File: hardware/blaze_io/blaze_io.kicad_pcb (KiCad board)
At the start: 4 copper layers, 70 x 70 mm, 58 parts, among them J1 Conn_01x30_Pin, J2 Conn_01x30_Socket, J3 Conn_01x04, J4 Conn_01x04, J5 Conn_01x03_Pin, J6 Conn_01x03_Pin, J7 Conn_01x03_Pin, J8 Conn_01x03_Pin, J9 JTAG, Q1 AO4892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

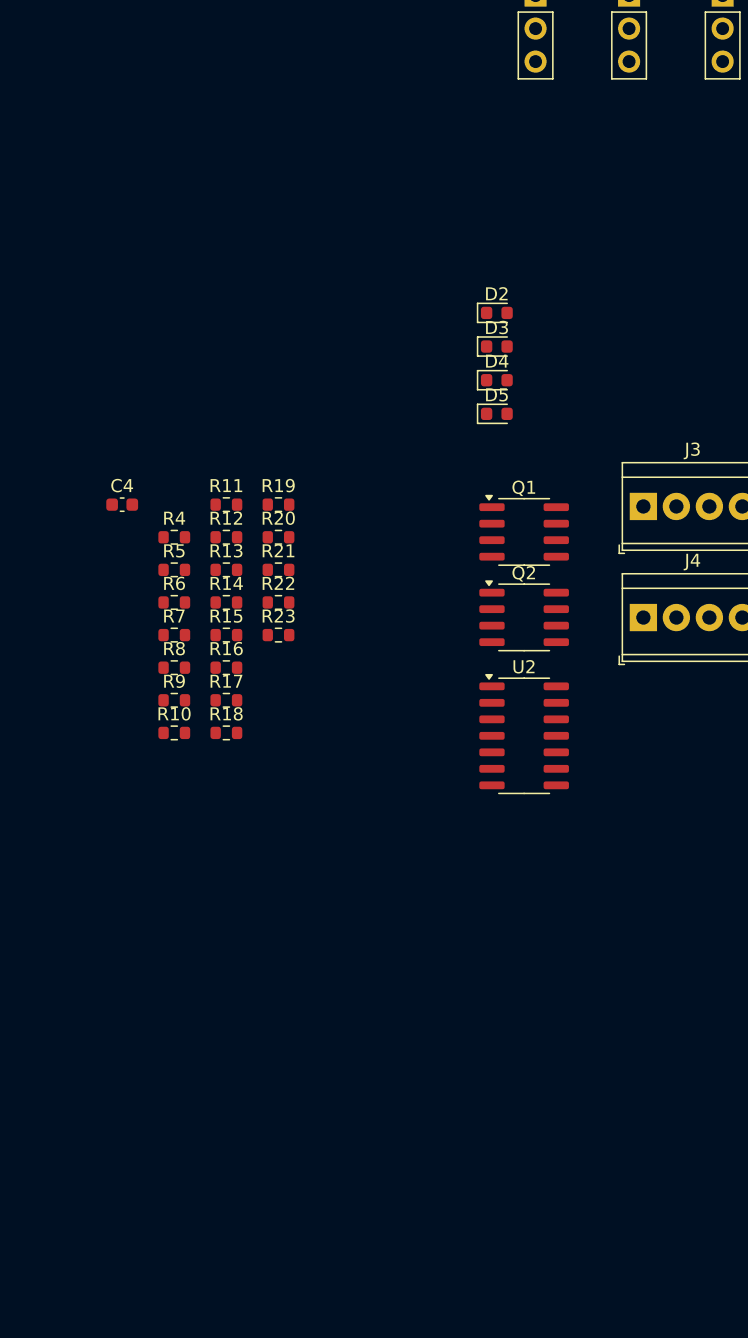
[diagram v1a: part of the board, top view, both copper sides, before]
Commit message: Pyro grouping
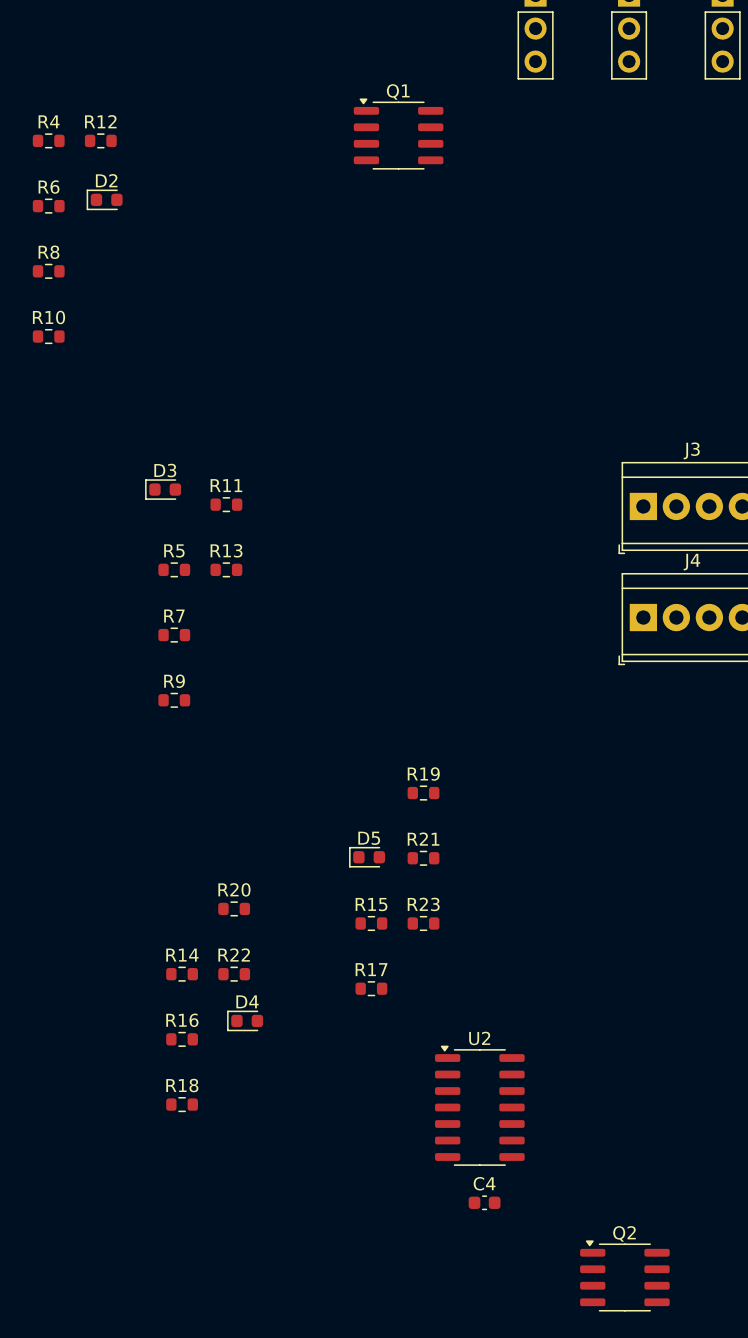
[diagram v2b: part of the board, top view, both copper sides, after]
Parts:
- moved C4 60.5 mm to (48.8, 182.8)
- moved D4 52.9 mm to (30.5, 168.8)
- moved Q2 51.4 mm to (59.6, 188.6)
- moved D5 35.5 mm to (39.9, 156.2)
- moved R8 32.0 mm to (15.2, 111.1)
- moved R6 32.0 mm to (15.2, 106.1)
- moved Q1 32.0 mm to (42.2, 100.7)
- moved R10 32.0 mm to (15.2, 116.1)
- moved R12 32.0 mm to (19.2, 101.1)
- moved R4 32.0 mm to (15.2, 101.1)
- moved D2 31.3 mm to (19.7, 105.6)
- moved U2 28.8 mm to (48.4, 175.5)
- moved R18 28.8 mm to (25.5, 175.2)
- moved R20 28.8 mm to (29.5, 160.2)
- moved R14 28.8 mm to (25.5, 165.2)
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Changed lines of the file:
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@@
 	(footprint "Package_SO:SOIC-8_3.9x4.9mm_P1.27mm"
 		(layer "F.Cu")
-		(at 51.82 131.16)
+		(at 42.155 100.65)
 		(descr "SOIC, 8 Pin (JEDEC MS-012AA, https://www.analog.com/media/en/package-pcb-resources/package/pkg_pdf/soic_narrow-r/r_8.pdf), generated with kicad-footprint-generator ipc_gullwing_generator.py")
 		(tags "SOIC SO")
@@
 	(footprint "Resistor_SMD:R_0603_1608Metric"
 		(layer "F.Cu")
-		(at 28.9 131.57)
+		(at 19.235 101.06)
 		(descr "Resistor SMD 0603 (1608 Metric), square (rectangular) end terminal, IPC_7351 nominal, (Body size source: IPC-SM-782 page 72, https://www.pcb-3d.com/wordpress/wp-content/uploads/ipc-sm-782a_amendment_1_and_2.pdf), generated with kicad-footprint-generator")
 		(tags "resistor")
@@
 	(footprint "Resistor_SMD:R_0603_1608Metric"
 		(layer "F.Cu")
-		(at 32.91 129.06)
+		(at 44.075 151.26)
 		(descr "Resistor SMD 0603 (1608 Metric), square (rectangular) end terminal, IPC_7351 nominal, (Body size source: IPC-SM-782 page 72, https://www.pcb-3d.com/wordpress/wp-content/uploads/ipc-sm-782a_amendment_1_and_2.pdf), generated with kicad-footprint-generator")
 		(tags "resistor")
@@
 	(footprint "LED_SMD:LED_0603_1608Metric"
 		(layer "F.Cu")
-		(at 49.72 114.3)
+		(at 19.6875 105.6)
 		(descr "LED SMD 0603 (1608 Metric), square (rectangular) end terminal, IPC_7351 nominal, (Body size source: http://www.tortai-tech.com/upload/download/2011102023233369053.pdf), generated with kicad-footprint-generator")
 		(tags "LED")
@@
 	(footprint "Resistor_SMD:R_0603_1608Metric"
 		(layer "F.Cu")
-		(at 32.91 136.59)
+		(at 29.5 165.2)
 		(descr "Resistor SMD 0603 (1608 Metric), square (rectangular) end terminal, IPC_7351 nominal, (Body size source: IPC-SM-782 page 72, https://www.pcb-3d.com/wordpress/wp-content/uploads/ipc-sm-782a_amendment_1_and_2.pdf), generated with kicad-footprint-generator")
 		(tags "resistor")
@@
 	(footprint "Resistor_SMD:R_0603_1608Metric"
 		(layer "F.Cu")
-		(at 24.89 136.59)
+		(at 15.225 106.08)
 		(descr "Resistor SMD 0603 (1608 Metric), square (rectangular) end terminal, IPC_7351 nominal, (Body size source: IPC-SM-782 page 72, https://www.pcb-3d.com/wordpress/wp-content/uploads/ipc-sm-782a_amendment_1_and_2.pdf), generated with kicad-footprint-generator")
 		(tags "resistor")
@@
 	(footprint "Package_SO:SOIC-14_3.9x8.7mm_P1.27mm"
 		(layer "F.Cu")
-		(at 51.82 146.855)
+		(at 48.41 175.465)
 		(descr "SOIC, 14 Pin (JEDEC MS-012AB, https://www.analog.com/media/en/package-pcb-resources/package/pkg_pdf/soic_narrow-r/r_14.pdf), generated with kicad-footprint-generator ipc_gullwing_generator.py")
 		(tags "SOIC SO")
@@
 	(footprint "Resistor_SMD:R_0603_1608Metric"
 		(layer "F.Cu")
-		(at 32.91 134.08)
+		(at 44.075 156.28)
 		(descr "Resistor SMD 0603 (1608 Metric), square (rectangular) end terminal, IPC_7351 nominal, (Body size source: IPC-SM-782 page 72, https://www.pcb-3d.com/wordpress/wp-content/uploads/ipc-sm-782a_amendment_1_and_2.pdf), generated with kicad-footprint-generator")
 		(tags "resistor")
@@
 	(footprint "Resistor_SMD:R_0603_1608Metric"
 		(layer "F.Cu")
-		(at 28.9 139.1)
+		(at 40.065 161.3)
 		(descr "Resistor SMD 0603 (1608 Metric), square (rectangular) end terminal, IPC_7351 nominal, (Body size source: IPC-SM-782 page 72, https://www.pcb-3d.com/wordpress/wp-content/uploads/ipc-sm-782a_amendment_1_and_2.pdf), generated with kicad-footprint-generator")
 		(tags "resistor")
@@
 	(footprint "Package_SO:SOIC-8_3.9x4.9mm_P1.27mm"
 		(layer "F.Cu")
-		(at 51.82 137.74)
+		(at 59.575 188.55)
 		(descr "SOIC, 8 Pin (JEDEC MS-012AA, https://www.analog.com/media/en/package-pcb-resources/package/pkg_pdf/soic_narrow-r/r_8.pdf), generated with kicad-footprint-generator ipc_gullwing_generator.py")
 		(tags "SOIC SO")
@@
 	(footprint "Resistor_SMD:R_0603_1608Metric"
 		(layer "F.Cu")
-		(at 24.89 141.61)
+		(at 15.225 111.1)
 		(descr "Resistor SMD 0603 (1608 Metric), square (rectangular) end terminal, IPC_7351 nominal, (Body size source: IPC-SM-782 page 72, https://www.pcb-3d.com/wordpress/wp-content/uploads/ipc-sm-782a_amendment_1_and_2.pdf), generated with kicad-footprint-generator")
 		(tags "resistor")
@@
 	(footprint "Resistor_SMD:R_0603_1608Metric"
 		(layer "F.Cu")
-		(at 32.91 139.1)
+		(at 44.075 161.3)
 		(descr "Resistor SMD 0603 (1608 Metric), square (rectangular) end terminal, IPC_7351 nominal, (Body size source: IPC-SM-782 page 72, https://www.pcb-3d.com/wordpress/wp-content/uploads/ipc-sm-782a_amendment_1_and_2.pdf), generated with kicad-footprint-generator")
 		(tags "resistor")
@@
 	(footprint "Resistor_SMD:R_0603_1608Metric"
 		(layer "F.Cu")
-		(at 24.89 146.63)
+		(at 15.225 116.12)
 		(descr "Resistor SMD 0603 (1608 Metric), square (rectangular) end terminal, IPC_7351 nominal, (Body size source: IPC-SM-782 page 72, https://www.pcb-3d.com/wordpress/wp-content/uploads/ipc-sm-782a_amendment_1_and_2.pdf), generated with kicad-footprint-generator")
 		(tags "resistor")
@@
 	(footprint "Capacitor_SMD:C_0603_1608Metric"
 		(layer "F.Cu")
-		(at 20.88 129.06)
+		(at 48.775 182.8)
 		(descr "Capacitor SMD 0603 (1608 Metric), square (rectangular) end terminal, IPC_7351 nominal, (Body size source: IPC-SM-782 page 76, https://www.pcb-3d.com/wordpress/wp-content/uploads/ipc-sm-782a_amendment_1_and_2.pdf), generated with kicad-footprint-generator")
 		(tags "capacitor")
@@
 	(footprint "Resistor_SMD:R_0603_1608Metric"
 		(layer "F.Cu")
-		(at 24.89 131.57)
+		(at 15.225 101.06)
 		(descr "Resistor SMD 0603 (1608 Metric), square (rectangular) end terminal, IPC_7351 nominal, (Body size source: IPC-SM-782 page 72, https://www.pcb-3d.com/wordpress/wp-content/uploads/ipc-sm-782a_amendment_1_and_2.pdf), generated with kicad-footprint-generator")
 		(tags "resistor")
@@
 	(footprint "LED_SMD:LED_0603_1608Metric"
 		(layer "F.Cu")
-		(at 49.72 119.48)
+		(at 30.5 168.8)
 		(descr "LED SMD 0603 (1608 Metric), square (rectangular) end terminal, IPC_7351 nominal, (Body size source: http://www.tortai-tech.com/upload/download/2011102023233369053.pdf), generated with kicad-footprint-generator")
 		(tags "LED")
@@
 	(footprint "LED_SMD:LED_0603_1608Metric"
 		(layer "F.Cu")
-		(at 49.72 116.89)
+		(at 24.1875 127.9)
 		(descr "LED SMD 0603 (1608 Metric), square (rectangular) end terminal, IPC_7351 nominal, (Body size source: http://www.tortai-tech.com/upload/download/2011102023233369053.pdf), generated with kicad-footprint-generator")
 		(tags "LED")
@@
 	(footprint "LED_SMD:LED_0603_1608Metric"
 		(layer "F.Cu")
-		(at 49.72 122.07)
+		(at 39.8875 156.2)
 		(descr "LED SMD 0603 (1608 Metric), square (rectangular) end terminal, IPC_7351 nominal, (Body size source: http://www.tortai-tech.com/upload/download/2011102023233369053.pdf), generated with kicad-footprint-generator")
 		(tags "LED")
@@
 	(footprint "Resistor_SMD:R_0603_1608Metric"
 		(layer "F.Cu")
-		(at 28.9 144.12)
+		(at 40.065 166.32)
 		(descr "Resistor SMD 0603 (1608 Metric), square (rectangular) end terminal, IPC_7351 nominal, (Body size source: IPC-SM-782 page 72, https://www.pcb-3d.com/wordpress/wp-content/uploads/ipc-sm-782a_amendment_1_and_2.pdf), generated with kicad-footprint-generator")
 		(tags "resistor")
@@
 	(footprint "Resistor_SMD:R_0603_1608Metric"
 		(layer "F.Cu")
-		(at 32.91 131.57)
+		(at 29.5 160.18)
 		(descr "Resistor SMD 0603 (1608 Metric), square (rectangular) end terminal, IPC_7351 nominal, (Body size source: IPC-SM-782 page 72, https://www.pcb-3d.com/wordpress/wp-content/uploads/ipc-sm-782a_amendment_1_and_2.pdf), generated with kicad-footprint-generator")
 		(tags "resistor")
@@
 	(footprint "Resistor_SMD:R_0603_1608Metric"
 		(layer "F.Cu")
-		(at 28.9 141.61)
+		(at 25.49 170.22)
 		(descr "Resistor SMD 0603 (1608 Metric), square (rectangular) end terminal, IPC_7351 nominal, (Body size source: IPC-SM-782 page 72, https://www.pcb-3d.com/wordpress/wp-content/uploads/ipc-sm-782a_amendment_1_and_2.pdf), generated with kicad-footprint-generator")
 		(tags "resistor")
@@
 	(footprint "Resistor_SMD:R_0603_1608Metric"
 		(layer "F.Cu")
-		(at 28.9 146.63)
+		(at 25.49 175.24)
 		(descr "Resistor SMD 0603 (1608 Metric), square (rectangular) end terminal, IPC_7351 nominal, (Body size source: IPC-SM-782 page 72, https://www.pcb-3d.com/wordpress/wp-content/uploads/ipc-sm-782a_amendment_1_and_2.pdf), generated with kicad-footprint-generator")
 		(tags "resistor")
@@
 	(footprint "Resistor_SMD:R_0603_1608Metric"
 		(layer "F.Cu")
-		(at 28.9 136.59)
+		(at 25.49 165.2)
 		(descr "Resistor SMD 0603 (1608 Metric), square (rectangular) end terminal, IPC_7351 nominal, (Body size source: IPC-SM-782 page 72, https://www.pcb-3d.com/wordpress/wp-content/uploads/ipc-sm-782a_amendment_1_and_2.pdf), generated with kicad-footprint-generator")
 		(tags "resistor")

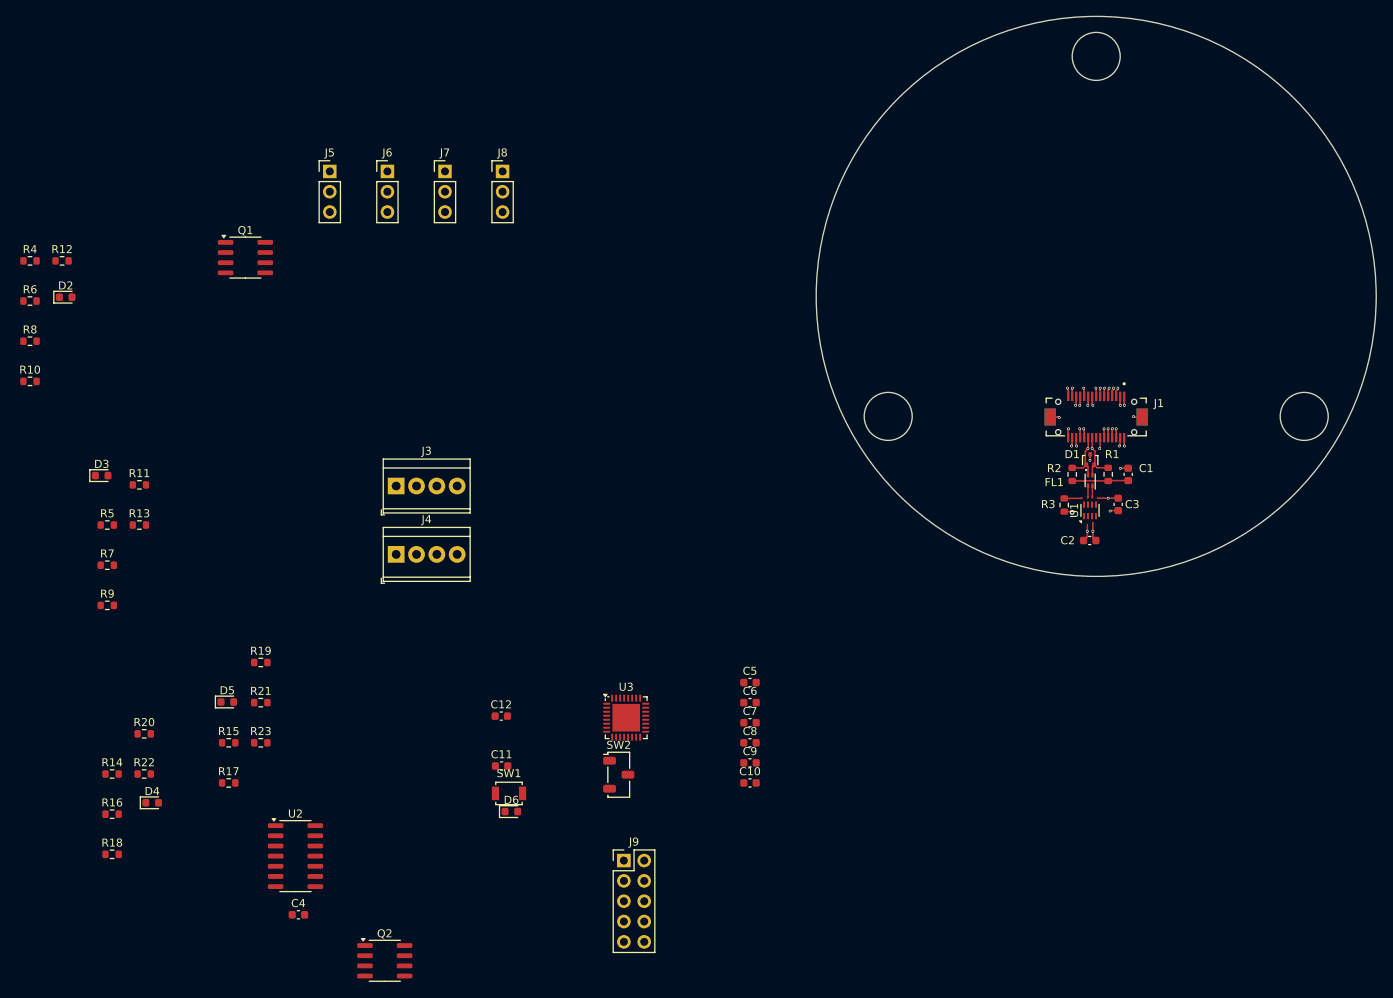
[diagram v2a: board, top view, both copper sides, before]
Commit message: Component layout
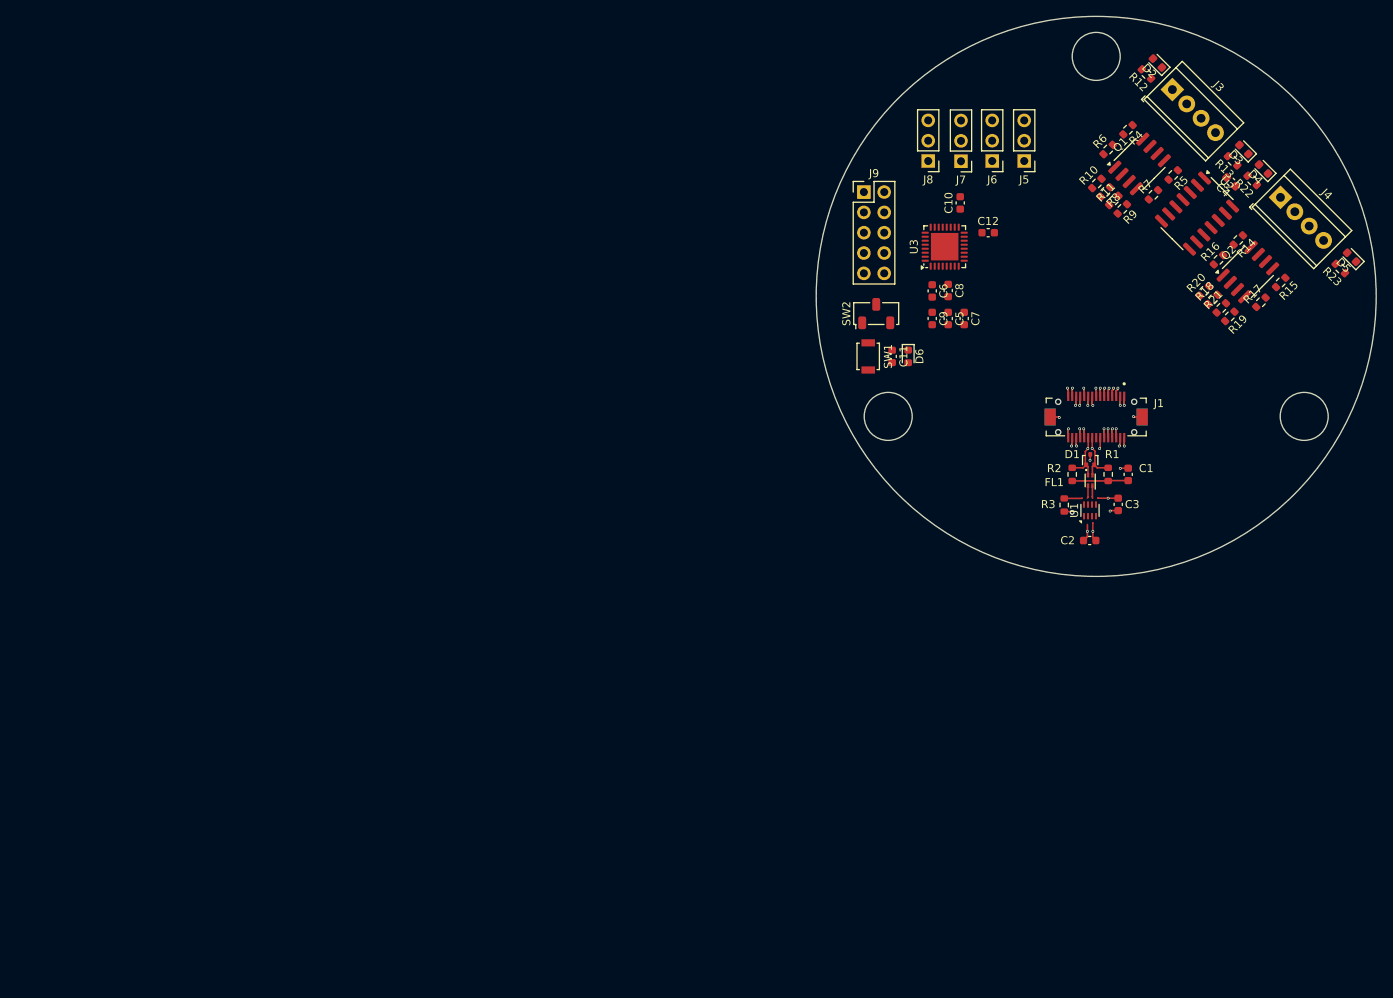
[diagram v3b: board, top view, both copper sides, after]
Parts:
- moved D4 159.9 mm to (169.4, 89.6), turned to 135 degrees
- moved R22 157.1 mm to (168.0, 91.0), turned to 135 degrees
- moved R14 155.8 mm to (166.3, 98.5), turned to -135 degrees
- moved R16 154.7 mm to (163.8, 100.9), turned to 45 degrees
- moved R18 154.1 mm to (163.1, 105.9), turned to 45 degrees
- moved D5 151.1 mm to (180.4, 100.6), turned to 135 degrees
- moved D3 148.5 mm to (167.0, 87.1), turned to 135 degrees
- moved C4 148.3 mm to (165.4, 91.2), turned to 135 degrees
- moved R23 147.4 mm to (179.0, 102.0), turned to 135 degrees
- moved R13 144.0 mm to (165.6, 88.6), turned to 135 degrees
- moved R20 143.6 mm to (162.0, 104.8), turned to 45 degrees
- moved R15 143.5 mm to (171.6, 103.8), turned to -135 degrees
- moved R17 142.3 mm to (169.1, 106.2), turned to 45 degrees
- moved R5 140.2 mm to (158.1, 90.3), turned to -135 degrees
- moved D2 139.6 mm to (156.2, 76.3), turned to 135 degrees
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
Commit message: PCB Work
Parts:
- turned D3 to -45 degrees
- turned D5 to -45 degrees
- turned R13 to -45 degrees
- turned R18 to -135 degrees
- turned R23 to -45 degrees
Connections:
- J1 pad 25: Net-(J1-Pin_25) -> +5V
- J1 pad 26: Net-(J1-Pin_26) -> +5V
- J2 pad 5: Net-(J1-Pin_26) -> +5V
- J2 pad 6: Net-(J1-Pin_25) -> +5V
- J3 pad 1: GND -> VBATT
- J3 pad 3: GND -> VBATT
- J4 pad 1: GND -> VBATT
- J4 pad 3: GND -> VBATT
- R10 pad 1: /FET_A -> Net-(R10-Pad1)
- R12 pad 1: /FET_A -> Net-(R10-Pad1)
- R18 pad 2: /FET_C -> Net-(R18-Pad2)
- R20 pad 1: /FET_C -> Net-(R18-Pad2)
- R22 pad 1: /FET_C -> Net-(R18-Pad2)
- R8 pad 2: /FET_A -> Net-(R10-Pad1)
- U2 pad 10: /FET_C -> Net-(R18-Pad2)
- U2 pad 3: /FET_A -> Net-(R10-Pad1)
- U3 pad 10: /FET_A_SENSE -> /FET_D_SENSE
- U3 pad 11: /FET_B_SENSE -> /FET_C_SENSE
- U3 pad 12: /FET_C_SENSE -> /FET_B_SENSE
- U3 pad 13: /FET_D_SENSE -> /FET_A_SENSE
- U3 pad 6: /FET_A -> /FET_C
- U3 pad 7: /FET_B -> /FET_D
- U3 pad 8: /FET_C -> /FET_A
- U3 pad 9: /FET_D -> /FET_B
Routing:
- net VBATT: track 4.53 -> 65.4 mm
- net GND: track 18.2 -> 73.1 mm, vias 10 -> 21
- net /CANRX: track 0.00 -> 54.6 mm
- net +5V: track 33.1 -> 84.8 mm, vias 7 -> 6
- net /CANTX: track 0.00 -> 46.8 mm
- net /FET_D_SENSE: track 0.00 -> 43.7 mm, vias 0 -> 2
- net /ARM: track 2.10 -> 40.1 mm, vias 1 -> 4
- net /FET_D: track 0.00 -> 37.7 mm
- net /FET_A: track 0.00 -> 36.3 mm
- net /FET_C_SENSE: track 0.00 -> 35.8 mm, vias 0 -> 2
- net /FET_C: track 0.00 -> 33.6 mm
- net /FET_B_SENSE: track 0.00 -> 31.6 mm, vias 0 -> 2
- net Net-(R10-Pad1): track 0.00 -> 31.6 mm
- net Net-(R19-Pad2): track 0.00 -> 30.8 mm
- net /PPS: track 2.33 -> 32.5 mm, vias 1 -> 2
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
